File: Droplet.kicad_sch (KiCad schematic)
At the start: 31 parts, among them Q1 BSS138W_C28646265, Q2 BSS138W_C28646265, Q3 BSS138W_C28646265, Q4 BSS138W_C28646265, U1 ATtiny202-SSNR, U2 IRM-H638T/TR2, U3 PAM2803AAF095, U4 MBKK1608T1R5M

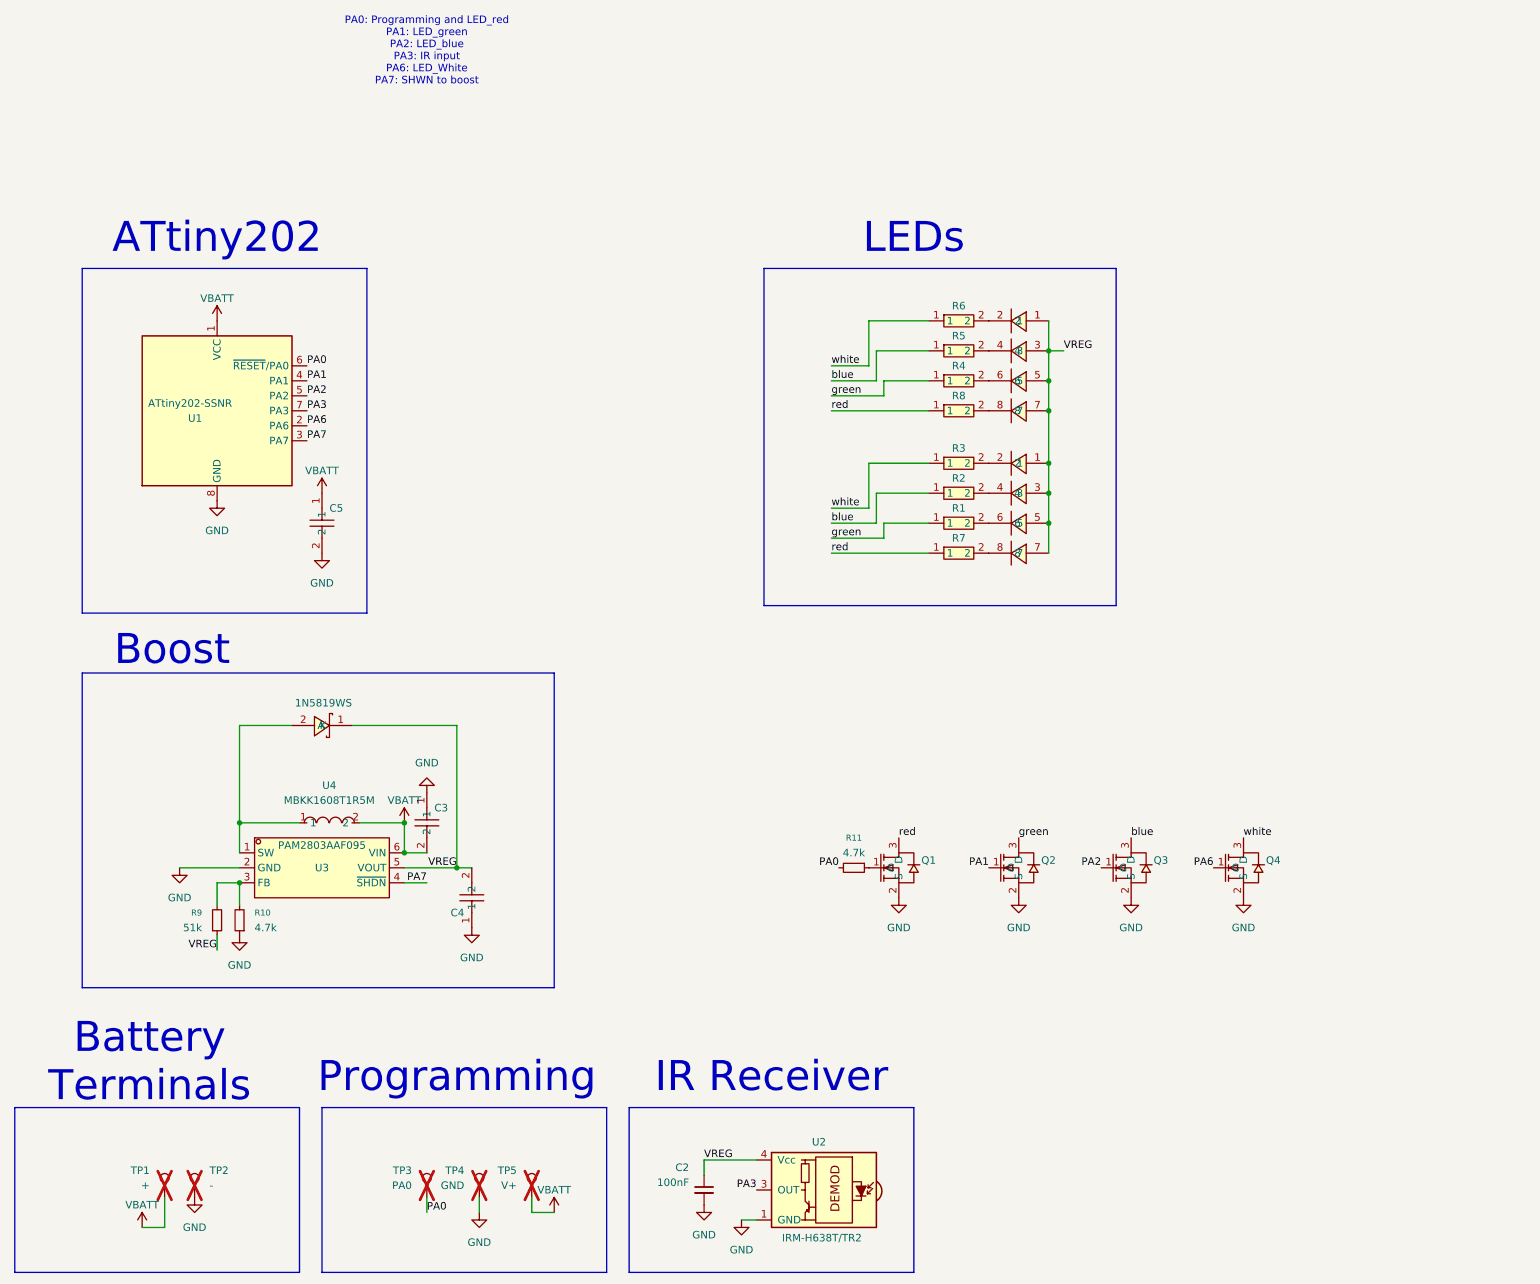
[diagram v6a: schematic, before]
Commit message: add boost, rework for flex pcb, order
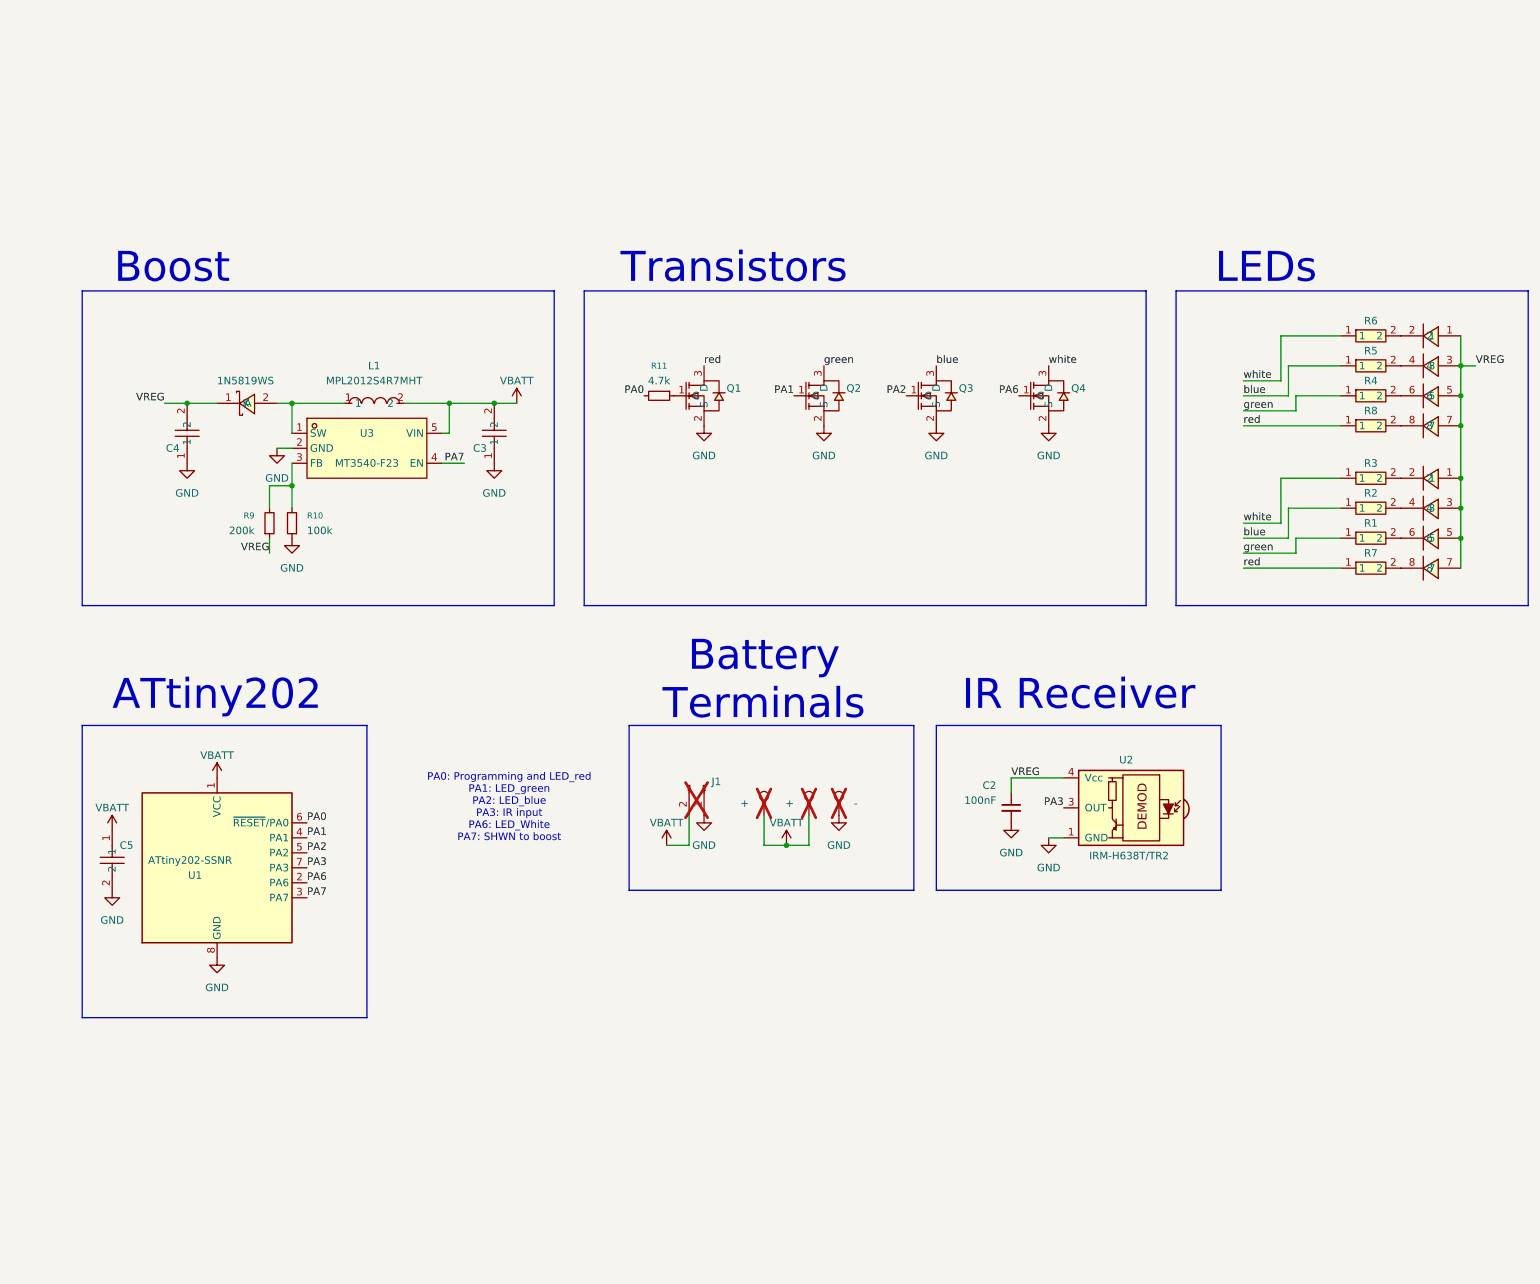
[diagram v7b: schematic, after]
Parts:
- removed TP4: GND, TestPoint:TestPoint_Pad_D1.5mm, symbol Connector:TestPoint
- removed TP5: V+, TestPoint:TestPoint_Pad_D1.5mm, symbol Connector:TestPoint
- removed U3: PAM2803AAF095, easyeda2kicad:SOT-23-6_L2.9-W1.6-P0.95-LS2.8-BR, symbol easyeda2kicad:PAM2803AAF095
- removed U4: MBKK1608T1R5M, easyeda2kicad:L0603, symbol easyeda2kicad:MBKK1608T1R5M
- added J1: Conn_01x02_Pin, Connector_PinHeader_2.54mm:PinHeader_1x02_P2.54mm_Vertical, symbol Connector:Conn_01x02_Pin
- added L1: MPL2012S4R7MHT, easyeda2kicad:L0805, symbol easyeda2kicad:MPL2012S4R7MHT
- added U3: MT3540-F23, easyeda2kicad:SOT-23-5_L3.0-W1.7-P0.95-LS2.8-BR, symbol easyeda2kicad:MT3540-F23
- R10: value 4.7k -> 100k
- R9: value 51k -> 200k
- TP1, TP2: footprint TestPoint:TestPoint_Pad_D4.0mm -> TestPoint:TestPoint_Pad_D6.0mm
- TP3: value PA0 -> +; footprint TestPoint:TestPoint_Pad_D1.5mm -> TestPoint:TestPoint_Pad_D2.0mm
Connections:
- net GND: now also J1.1 (Pin_1), U3.2 (GND)
- net PA0: no longer TP3.1
- net PA7: now also U3.4 (EN)
- net VBATT: now also TP3.1, J1.2 (Pin_2), L1.2, U3.5 (VIN)
- net at D3.2 (A): now also L1.1, U3.1 (SW)
- net at R10.2, R9.2: now also U3.3 (FB)
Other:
- note added: "Transistors"
- note removed: "Programming"
- moved on the sheet: C2, C3, C5, Q1, Q2, Q3, Q4, R1, R10, R11, R2, R3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
